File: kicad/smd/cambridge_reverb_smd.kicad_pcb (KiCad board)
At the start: 2 copper layers, 155 x 90 mm, 181 parts, among them IC1 TL072CP, IC2 TL072CP, IC3 TL074CN, Q1 MMBF5457, Q2 MMBF5457, T1 reuse / AnTek AS-0524, U1 LM317T

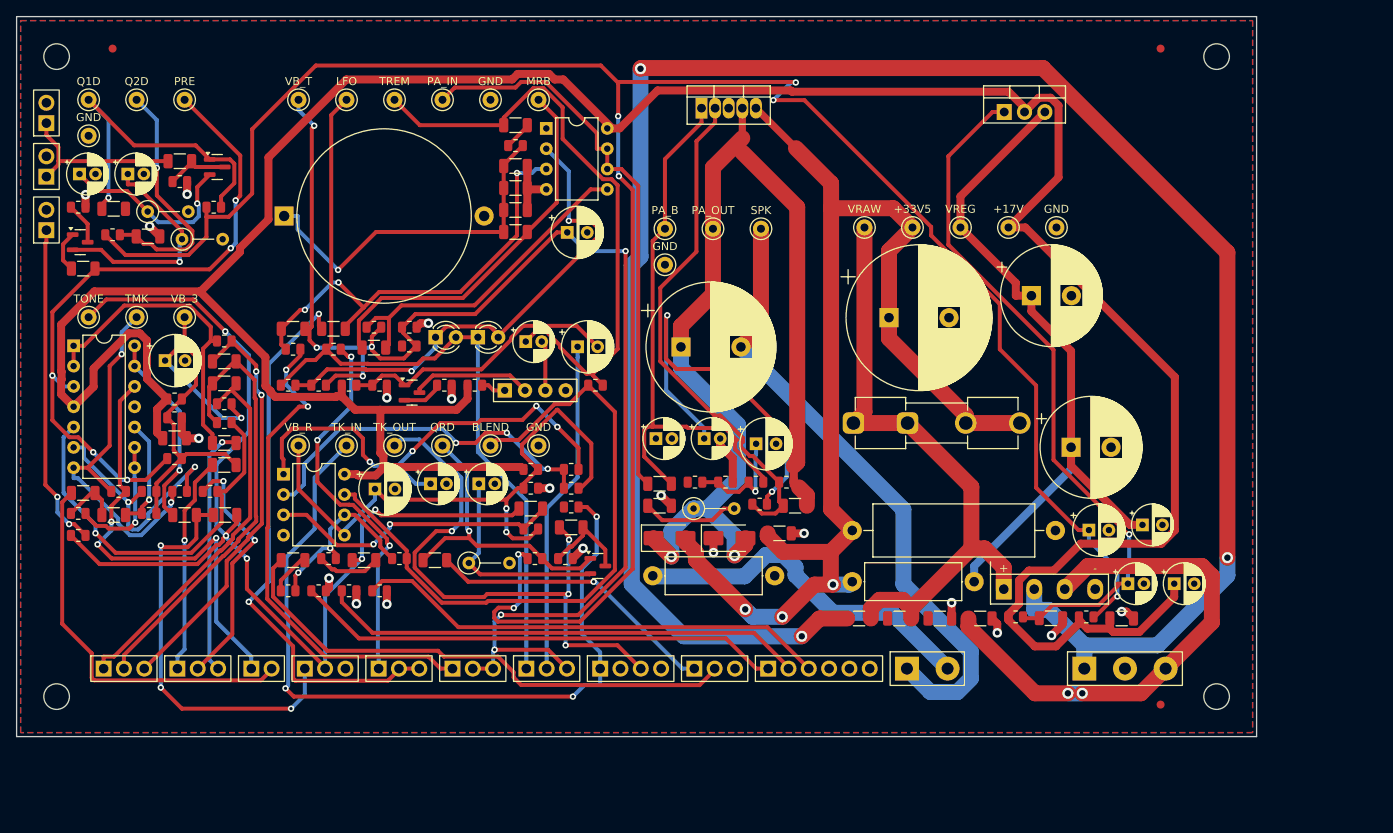
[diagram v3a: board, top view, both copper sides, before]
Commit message: Four-layer boards, no routes through footprints, rules by impedance, RF stoppers
Both boards move to a 4-layer stack (JLC04161H-7628): F.Cu signal, In1 solid GND
plane, In2 inner signal layer, B.Cu signal + shield-only GND pour, locked perimeter
GND stitching vias every 15 mm. Outer traces sit 0.21 mm from the plane instead of
1.5 mm; the long runs live on In2 under the plane and the outer layers carry escapes.

- No routes through footprints: gen_pcb writes keepout rule areas (kp_<ref>, tracks;
  vias too under SMD parts; component side) between every part's pads -- pin-to-pin
  strips and the body between rows -- with same-net pin gaps exempt and power-only
  parts exempt. 155 / 147 areas. Freerouting gets them as keepouts, KiCad DRC checks.
- Rules by impedance: new HiZ net class (0.3 mm; gates, RF nodes, tone ladder and
  wipers, LFO timing, MRB tank, PA + input), Default = low-Z signal, Power 1.0 mm,
  HighCurrent 1.5 mm, TankDrive; .kicad_dru: HighCurrent >= 0.6 mm from any signal
  trace, tank drive >= 0.8 mm from the return (SMD 0.4 / 0.6), tracks and vias only;
  route_board hands the router the same per-class clearances.
- RF stoppers R_rf1/C_rf1 (1k + 100 pF) at Q1's gate and R_rf2/C_rf2 at the recovery
  JFET's gate (the guitar and tank cables are the antennas). Noise floor unchanged.
- route_board: strips the plane layer from the DSN (Freerouting 1.9 ignores
  (active off) and routed 7 m of copper on the planes; typed as a power layer it
  treated every through-hole pad as connected), routes inner signal layers, per-board
  class clearances, 4-layer defaults.
- SMD board 170x100 mm, 1.2 mm gap (was 155x90 / 0.5): with the keepouts every SMD
  ground / rail pad needs a via beside it and none fitted; smaller SMD rail vias.
  THT gap 1.6 mm. Placer: gaps are the routing channels now.
- Crosstalk audit knows the 4-layer geometry; cost model notes the 4-layer PCB.

Routing: THT 218/226, 0 DRC errors, 0 rule hits; SMD 216/226, 1 starved thermal.
Crosstalk aft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
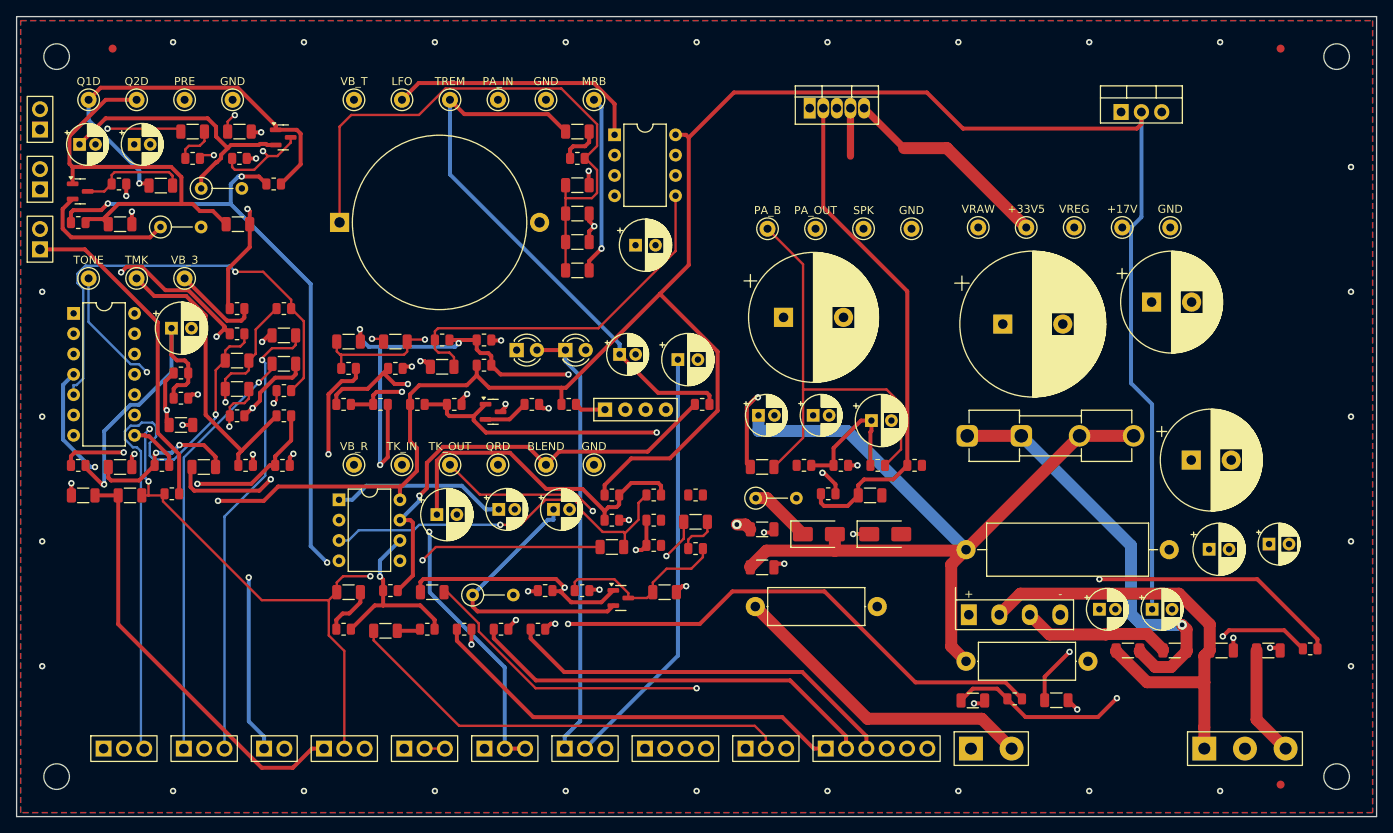
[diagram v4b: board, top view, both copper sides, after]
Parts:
- added C_rf1: 100pF, C_1206_3216Metric, F.Cu at (27.9, 14.4)
- added C_rf2: 100pF, C_1206_3216Metric, F.Cu at (81.0, 72.0)
- added R_rf1: 1k, R_0805_2012Metric, F.Cu at (22.0, 17.7)
- added R_rf2: 1k, R_0805_2012Metric, F.Cu at (84.9, 66.5)
- moved R_reg1 37.0 mm to (161.7, 79.0)
- moved C104 36.2 mm to (156.5, 79.2)
- moved C103 35.4 mm to (150.6, 79.2)
- moved C102 34.6 mm to (144.8, 79.2)
- moved C101 33.9 mm to (138.9, 79.2)
- moved TP_GND_PA 31.1 mm to (111.9, 26.5)
- moved C_reg_out2 21.2 mm to (119.5, 85.5)
- moved R_fs_mrb 20.4 mm to (65.2, 76.6)
- moved R_inb 20.3 mm to (27.6, 36.5)
- moved C_cpl_out 20.1 mm to (27.7, 25.9)
- moved R_fs_trem 19.6 mm to (60.6, 76.6)
- moved D2 19.5 mm to (108.6, 64.7)
- moved R_fs_rev 18.8 mm to (55.9, 76.6)
- moved D1 18.7 mm to (100.3, 64.7)
- moved TP_GND_PRE 18.6 mm to (27.0, 10.4)
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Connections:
- C_in_pre pad 2: Q1G -> RF1
- C_rev2 pad 2: QRG -> RF2
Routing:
- net AC1: track 253.9 -> 57.5 mm, vias 3 -> 0
- net +17V_PRE: track 289.9 -> 177.9 mm, vias 7 -> 5
- net PA_OUT: track 129.5 -> 51.2 mm, vias 2 -> 0
- net TANK_IN: track 99.6 -> 49.8 mm, vias 3 -> 0
- net LFO_OUT: track 104.8 -> 149.8 mm, vias 0 -> 1
- net PA_GAIN: track 51.7 -> 11.1 mm, vias 3 -> 1
- net VBIAS_3: track 54.4 -> 94.6 mm, vias 1 -> 3
- net R_DRVO: track 58.2 -> 21.9 mm, vias 4 -> 0
- net MRB_T: track 45.0 -> 72.8 mm, vias 1 -> 0
- net VRAW: track 77.6 -> 105.2 mm, vias 0 -> 1
- net ADJ17: track 87.4 -> 113.8 mm, vias 1 -> 2
- net JTA: track 31.2 -> 57.2 mm
- net JTB: track 27.3 -> 52.7 mm
- net BLEND: track 82.5 -> 58.0 mm, vias 0 -> 1
- net +17V: track 388.4 -> 366.8 mm, vias 0 -> 5
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- added copper zone on In1.Cu, net GND
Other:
- board size 155 x 90 mm -> 170 x 100 mm
- copper layers 2 -> 4
